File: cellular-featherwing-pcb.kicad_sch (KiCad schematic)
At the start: 69 parts, among them J1 SIM8060-6-0-14-00-A, J2 TSM-116-01-L-SV, J3 TSM-112-01-L-SV, J4 U.FL-R-SMT, U1 BG96, U2 TPS63020QDSJTQ1, U3 TXB0108DQSR, U4 MAX8868EUK30+T

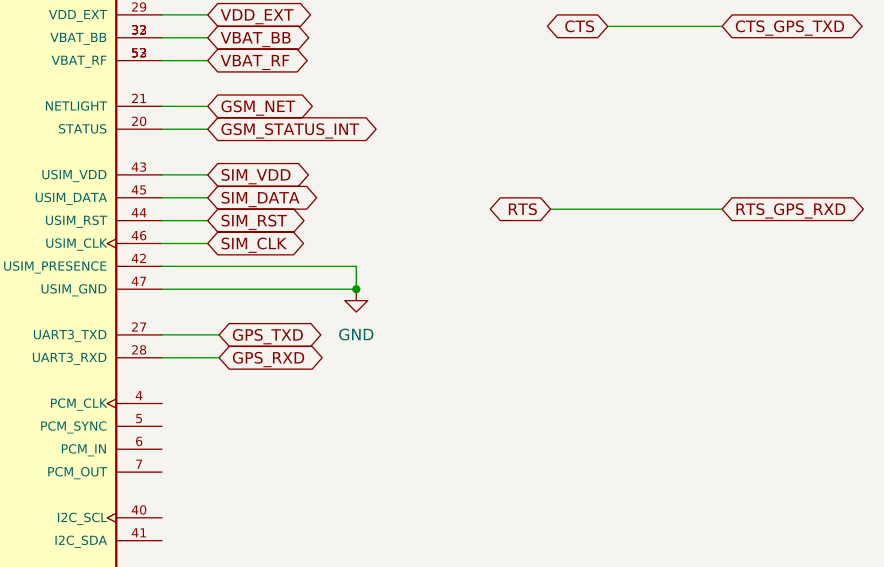
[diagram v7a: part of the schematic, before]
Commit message: All items routed
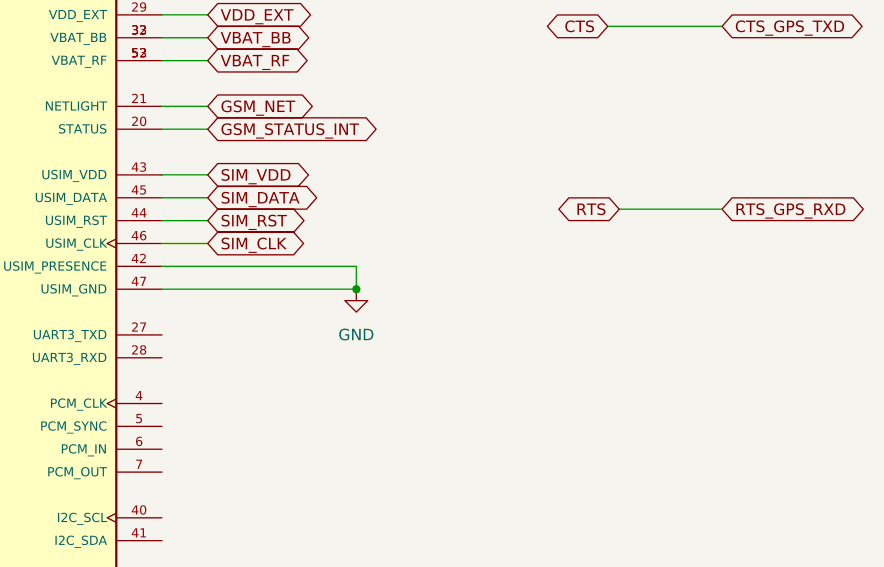
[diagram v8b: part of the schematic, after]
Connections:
- net GPS_RXD: no longer names the net of U1.28 (UART3_RXD)
- net GPS_TXD: no longer names the net of U1.27 (UART3_TXD)
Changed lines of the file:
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@@
-    (stroke (width 0) (type default) (color 0 0 0 0))
-  )
-  (wire (pts (xy 234.95 130.81) (xy 241.3 130.81))
     (stroke (width 0) (type default) (color 0 0 0 0))
   )
@@
     (stroke (width 0) (type default) (color 0 0 0 0))
   )
-  (wire (pts (xy 234.95 133.35) (xy 241.3 133.35))
-    (stroke (width 0) (type default) (color 0 0 0 0))
-  )
   (wire (pts (xy 46.99 254) (xy 53.34 254))
     (stroke (width 0) (type default) (color 0 0 0 0))
@@
     (stroke (width 0) (type default) (color 0 0 0 0))
   )
-  (wire (pts (xy 278.13 116.84) (xy 297.18 116.84))
+  (wire (pts (xy 285.75 116.84) (xy 297.18 116.84))
     (stroke (width 0) (type default) (color 0 0 0 0))
   )
@@
     )
   )
-  (global_label "GPS_RXD" (shape bidirectional) (at 241.3 133.35 0) (fields_autoplaced)
-    (effects (font (size 1.27 1.27)) (justify left))
-    (property "Intersheet References" "${INTERSHEET_REFS}" (id 0) (at 252.1798 133.2706 0)
-      (effects (font (size 1.27 1.27)) (justify left) hide)
-    )
-  )
   (global_label "GSM_TXD_ESP_RTS" (shape bidirectional) (at 378.46 227.33 0) (fields_autoplaced)
     (effects (font (size 1.27 1.27)) (justify left))
@@
     )
   )
-  (global_label "RTS" (shape bidirectional) (at 278.13 116.84 180) (fields_autoplaced)
-    (effects (font (size 1.27 1.27)) (justify right))
-    (property "Intersheet References" "${INTERSHEET_REFS}" (id 0) (at 272.2698 116.7606 0)
+  (global_label "RTS" (shape bidirectional) (at 285.75 116.84 180) (fields_autoplaced)
+    (effects (font (size 1.27 1.27)) (justify right))
+    (property "Intersheet References" "${INTERSHEET_REFS}" (id 0) (at 279.8898 116.7606 0)
       (effects (font (size 1.27 1.27)) (justify right) hide)
     )
@@
     )
   )
-  (global_label "GPS_TXD" (shape bidirectional) (at 241.3 130.81 0) (fields_autoplaced)
-    (effects (font (size 1.27 1.27)) (justify left))
-    (property "Intersheet References" "${INTERSHEET_REFS}" (id 0) (at 251.8774 130.7306 0)
-      (effects (font (size 1.27 1.27)) (justify left) hide)
-    )
-  )
